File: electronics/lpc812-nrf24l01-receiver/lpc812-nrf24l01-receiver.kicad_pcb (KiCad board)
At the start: 2 copper layers, 25 x 24 mm, 21 parts, among them K1 BAT, K2 CH3, K3 TH, K4 ST, P1 NRF24L01+, SW1 ISP/BIND, U1 MCP1703T-3302E/CB, U2 LPC812M101JDH16_TSSOP16, X1 12 MHz

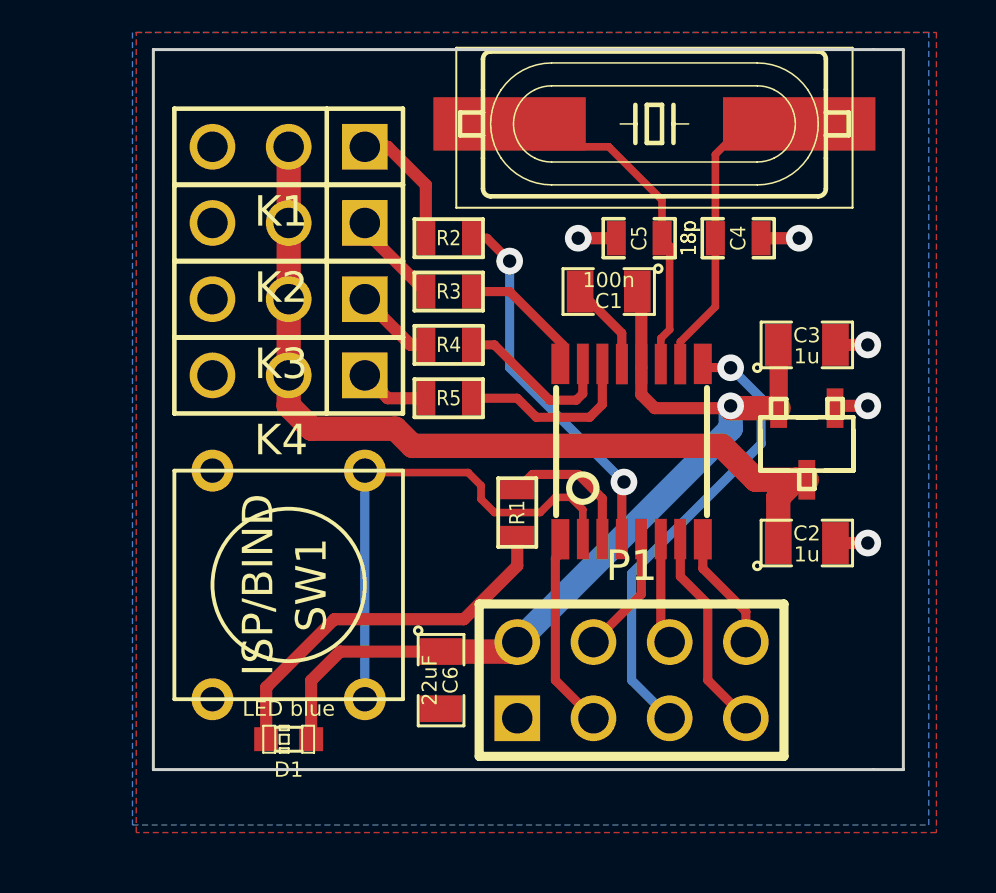
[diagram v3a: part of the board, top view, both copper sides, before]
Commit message: Start working on the silk screen
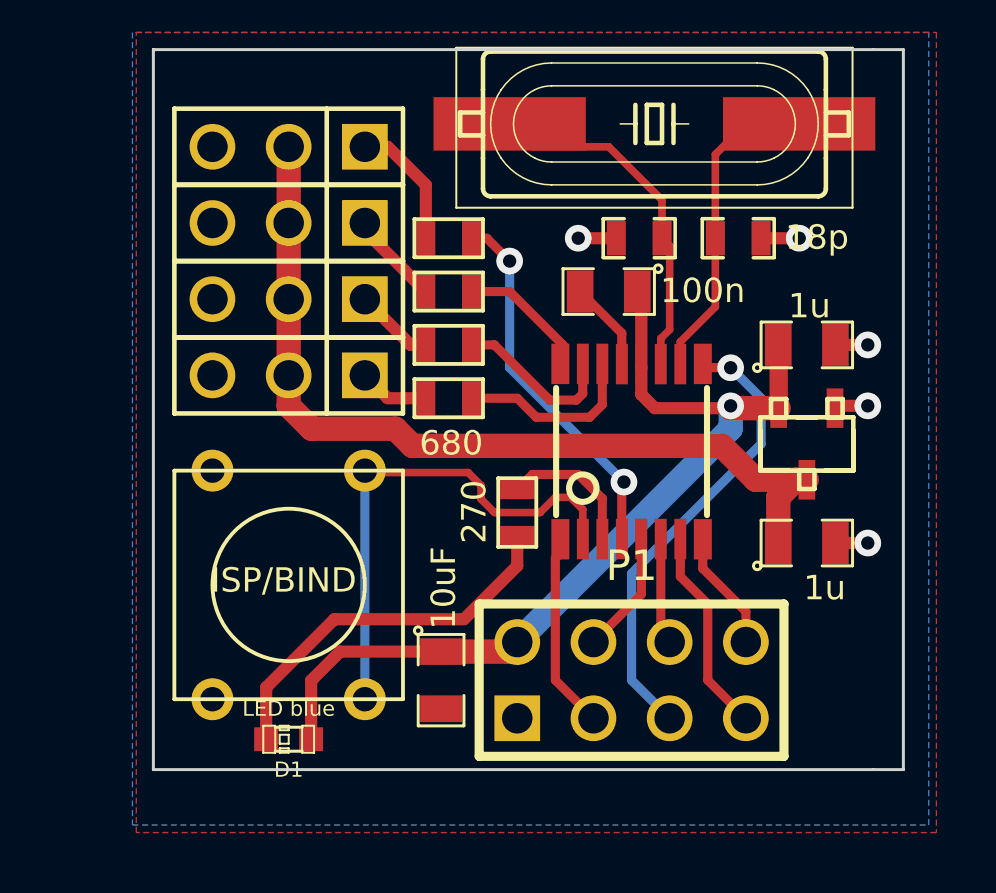
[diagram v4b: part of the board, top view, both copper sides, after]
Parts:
- C6: value 22uF -> 10uF
- U1: value MCP1703T-3302E/CB -> MCP1703
- U2: value LPC812M101JDH16_TSSOP16 -> LPC812
- X1: value 12 MHz -> 16 MHz
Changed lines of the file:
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@@
     (links 47)
     (no_connects 0)
-    (area 11.303 10.11555 55.524401 38.100001)
+    (area 55.372 10.16 96.592672 84.100001)
     (thickness 1.6)
     (drawings 6)
@@
     (22 B.Mask user)
     (23 F.Mask user)
-    (24 Dwgs.User user)
+    (24 Dwgs.User user hide)
     (25 Cmts.User user)
     (26 Eco1.User user)
@@
     (pad_to_mask_clearance 0)
     (aux_axis_origin 65 58)
-    (visible_elements 7FFFFFCF)
+    (visible_elements 7FFFFF9F)
     (pcbplotparams
       (layerselection 284721153)
@@
     (descr "Connecteur 3 pins")
     (tags "CONN DEV")
-    (fp_text reference K1 (at 0.254 -2.159 180) (layer F.SilkS)
+    (fp_text reference K1 (at 0.254 -2.159 180) (layer F.SilkS) hide
       (effects (font (size 1.016 1.016) (thickness 0.1524)))
     )
@@
     (descr "Connecteur 3 pins")
     (tags "CONN DEV")
-    (fp_text reference K2 (at 0.254 -2.159 180) (layer F.SilkS)
+    (fp_text reference K2 (at 0.254 -2.159 180) (layer F.SilkS) hide
       (effects (font (size 1.016 1.016) (thickness 0.1524)))
     )
@@
     (descr "Connecteur 3 pins")
     (tags "CONN DEV")
-    (fp_text reference K3 (at 0.254 -2.159 180) (layer F.SilkS)
+    (fp_text reference K3 (at 0.254 -2.159 180) (layer F.SilkS) hide
       (effects (font (size 1.016 1.016) (thickness 0.1524)))
     )
@@
     (descr "Connecteur 3 pins")
     (tags "CONN DEV")
-    (fp_text reference K4 (at 0.254 -2.159 180) (layer F.SilkS)
+    (fp_text reference K4 (at 0.254 -2.159 180) (layer F.SilkS) hide
       (effects (font (size 1.016 1.016) (thickness 0.1524)))
     )
@@
     (at 86.782 71.146 180)
     (attr smd)
-    (fp_text reference U1 (at 0.9652 -3.4544 180) (layer B.SilkS)
+    (fp_text reference U1 (at -7.198 -4.038 180) (layer B.SilkS) hide
       (effects (font (size 2.0828 2.0828) (thickness 0.0889)))
     )
-    (fp_text value MCP1703T-3302E/CB (at 0.5588 3.3782 180) (layer B.SilkS)
-      (effects (font (size 2.0828 2.0828) (thickness 0.0889)))
+    (fp_text value MCP1703 (at -2.372 0.026 270) (layer B.SilkS)
+      (effects (font (size 0.8128 0.8128) (thickness 0.2032)))
     )
     (fp_line (start -0.6858 0.889) (end -1.1938 0.889) (layer F.SilkS) (width 0.1524))
@@
     (at 84.496 64.288)
     (attr smd)
-    (fp_text reference C4 (at 0 0 90) (layer F.SilkS)
+    (fp_text reference C4 (at 0 0 90) (layer F.SilkS) hide
       (effects (font (size 0.508 0.4572) (thickness 0.1143)))
     )
-    (fp_text value 18p (at -1.651 0 90) (layer F.SilkS)
-      (effects (font (size 0.508 0.4572) (thickness 0.1143)))
+    (fp_text value 18p (at 2.626 -0.026) (layer F.SilkS)
+      (effects (font (size 0.8128 0.8128) (thickness 0.2032)))
     )
     (fp_line (start 0.50038 0.65024) (end 1.19888 0.65024) (layer F.SilkS) (width 0.11938))
@@
     (at 81.194 64.288 180)
     (attr smd)
-    (fp_text reference C5 (at 0 0 270) (layer F.SilkS)
-      (effects (font (size 0.508 0.4572) (thickness 0.1143)))
-    )
-    (fp_text value 18p (at -1.651 0 270) (layer F.SilkS)
-      (effects (font (size 0.508 0.4572) (thickness 0.1143)))
+    (fp_text reference C5 (at 0 0 270) (layer F.SilkS) hide
+      (effects (font (size 0.8128 0.8128) (thickness 0.000001)))
+    )
+    (fp_text value 18p (at -1.651 0 270) (layer F.SilkS) hide
+      (effects (font (size 0.8128 0.8128) (thickness 0.2032)))
     )
     (fp_line (start 0.50038 0.65024) (end 1.19888 0.65024) (layer F.SilkS) (width 0.11938))
@@
   (module SW_PUSH_SMALL (layer F.Cu)
     (at 69.51 75.845 270)
-    (fp_text reference SW1 (at 0 -0.762 270) (layer F.SilkS)
+    (fp_text reference SW1 (at 0 -0.762 270) (layer F.SilkS) hide
       (effects (font (size 1.016 1.016) (thickness 0.2032)))
     )
-    (fp_text value ISP/BIND (at 0 1.016 270) (layer F.SilkS)
-      (effects (font (size 1.016 1.016) (thickness 0.2032)))
+    (fp_text value ISP/BIND (at -0.153 0.168 360) (layer F.SilkS)
+      (effects (font (size 0.8128 0.8128) (thickness 0.2032)))
     )
     (fp_circle (center 0 0) (end 0 -2.54) (layer F.SilkS) (width 0.127))
@@
     (tags CRYSTAL)
     (attr smd)
-    (fp_text reference X1 (at -2.54 -3.302 180) (layer B.SilkS)
+    (fp_text reference X1 (at -2.54 -3.302 180) (layer B.SilkS) hide
       (effects (font (size 1.27 1.27) (thickness 0.0889)))
     )
-    (fp_text value "12 MHz" (at -1.905 3.429 180) (layer B.SilkS)
-      (effects (font (size 1.27 1.27) (thickness 0.0889)))
+    (fp_text value "16 MHz" (at 0.168 -1.752 180) (layer B.SilkS)
+      (effects (font (size 0.8128 0.8128) (thickness 0.2032)))
     )
     (fp_line (start -6.604 2.54) (end 6.604 2.54) (layer F.SilkS) (width 0.06604))
@@
     (at 74.59 79.02 270)
     (attr smd)
-    (fp_text reference C6 (at 0 -0.3175 270) (layer F.SilkS)
+    (fp_text reference C6 (at 0 -0.3175 270) (layer F.SilkS) hide
       (effects (font (size 0.50038 0.50038) (thickness 0.10922)))
     )
-    (fp_text value 22uF (at 0 0.381 270) (layer F.SilkS)
-      (effects (font (size 0.50038 0.50038) (thickness 0.10922)))
+    (fp_text value 10uF (at -3.074 -0.086 270) (layer F.SilkS)
+      (effects (font (size 0.8128 0.8128) (thickness 0.2032)))
     )
     (fp_circle (center -1.651 0.762) (end -1.651 0.635) (layer F.SilkS) (width 0.09906))
@@
     (at 74.844 64.288 180)
     (attr smd)
-    (fp_text reference R2 (at 0 0 180) (layer F.SilkS)
+    (fp_text reference R2 (at 0 0 180) (layer F.SilkS) hide
       (effects (font (size 0.508 0.4572) (thickness 0.1143)))
     )
@@
     (at 74.844 66.066 180)
     (attr smd)
-    (fp_text reference R3 (at 0 0 180) (layer F.SilkS)
+    (fp_text reference R3 (at 0 0 180) (layer F.SilkS) hide
       (effects (font (size 0.508 0.4572) (thickness 0.1143)))
     )
@@
     (at 74.844 67.844 180)
     (attr smd)
-    (fp_text reference R4 (at 0 0 180) (layer F.SilkS)
+    (fp_text reference R4 (at 0 0 180) (layer F.SilkS) hide
       (effects (font (size 0.508 0.4572) (thickness 0.1143)))
     )
@@
     (at 74.844 69.622 180)
     (attr smd)
-    (fp_text reference R5 (at 0 0 180) (layer F.SilkS)
+    (fp_text reference R5 (at 0 0 180) (layer F.SilkS) hide
       (effects (font (size 0.508 0.4572) (thickness 0.1143)))
     )
-    (fp_text value 680 (at 0 0 180) (layer F.SilkS) hide
-      (effects (font (size 0.508 0.4572) (thickness 0.1143)))
+    (fp_text value 680 (at -0.086 -1.498 180) (layer F.SilkS)
+      (effects (font (size 0.8128 0.8128) (thickness 0.2032)))
     )
     (fp_line (start -1.143 -0.635) (end 1.143 -0.635) (layer F.SilkS) (width 0.127))
@@
     (at 86.782 67.844)
     (attr smd)
-    (fp_text reference C3 (at 0 -0.3175) (layer F.SilkS)
-      (effects (font (size 0.50038 0.50038) (thickness 0.10922)))
-    )
-    (fp_text value 1u (at 0 0.381) (layer F.SilkS)
-      (effects (font (size 0.50038 0.50038) (thickness 0.10922)))
+    (fp_text reference C3 (at 0 -0.3175) (layer F.SilkS) hide
+      (effects (font (size 0.8128 0.8128) (thickness 0.10922)))
+    )
+    (fp_text value 1u (at 0.086 -1.296) (layer F.SilkS)
+      (effects (font (size 0.8128 0.8128) (thickness 0.2032)))
     )
     (fp_circle (center -1.651 0.762) (end -1.651 0.635) (layer F.SilkS) (width 0.09906))
@@
     (at 80.178 66.066 180)
     (attr smd)
-    (fp_text reference C1 (at 0 -0.3175 180) (layer F.SilkS)
+    (fp_text reference C1 (at 0 -0.3175 180) (layer F.SilkS) hide
       (effects (font (size 0.50038 0.50038) (thickness 0.10922)))
     )
-    (fp_text value 100n (at 0 0.381 180) (layer F.SilkS)
-      (effects (font (size 0.50038 0.50038) (thickness 0.10922)))
+    (fp_text value 100n (at -3.134 0.026 180) (layer F.SilkS)
+      (effects (font (size 0.8128 0.8128) (thickness 0.2032)))
     )
     (fp_circle (center -1.651 0.762) (end -1.651 0.635) (layer F.SilkS) (width 0.09906))
@@
     (at 86.782 74.448)
     (attr smd)
-    (fp_text reference C2 (at 0 -0.3175) (layer F.SilkS)
+    (fp_text reference C2 (at 0 -0.3175) (layer F.SilkS) hide
       (effects (font (size 0.50038 0.50038) (thickness 0.10922)))
     )
-    (fp_text value 1u (at 0 0.381) (layer F.SilkS)
-      (effects (font (size 0.50038 0.50038) (thickness 0.10922)))
+    (fp_text value 1u (at 0.594 1.498) (layer F.SilkS)
+      (effects (font (size 0.8128 0.8128) (thickness 0.2032)))
     )
     (fp_circle (center -1.651 0.762) (end -1.651 0.635) (layer F.SilkS) (width 0.09906))
@@
     (at 77.13 73.432 90)
     (attr smd)
-    (fp_text reference R1 (at 0 0 90) (layer F.SilkS)
+    (fp_text reference R1 (at 0 0 90) (layer F.SilkS) hide
       (effects (font (size 0.508 0.4572) (thickness 0.1143)))
     )
-    (fp_text value 270 (at 0 0 90) (layer F.SilkS) hide
-      (effects (font (size 0.508 0.4572) (thickness 0.1143)))
+    (fp_text value 270 (at 0.026 -1.438 90) (layer F.SilkS)
+      (effects (font (size 0.8128 0.8128) (thickness 0.2032)))
     )
     (fp_line (start -1.143 -0.635) (end 1.143 -0.635) (layer F.SilkS) (width 0.127))
@@
     (at 80.94 71.4)
     (descr "<b>Thin Shrink Small Outline Plastic 16</b><p>")
-    (fp_text reference U2 (at -3.302 -0.3556 90) (layer Eco1.User)
+    (fp_text reference U2 (at -3.302 -0.3556 90) (layer Eco1.User) hide
       (effects (font (size 0.8128 0.8128) (thickness 0.14478)))
     )
-    (fp_text value LPC812M101JDH16_TSSOP16 (at 2.921 0.8636 90) (layer Eco1.User)
-      (effects (font (size 0.4064 0.4064) (thickness 0.04064)))
+    (fp_text value LPC812 (at -0.041 -0.153) (layer Eco1.User)
+      (effects (font (size 0.8128 0.8128) (thickness 0.2032)))
     )
     (fp_line (start -2.5146 2.28092) (end 2.5146 2.28092) (layer Cmts.User) (width 0.2032))

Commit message: Tweak the footprints and board
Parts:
- U1: value MCP1703 -> MCP1703T-3302E/CB
- U2: value LPC812 -> LPC812M101JDH16
- X1: footprint crystal-SM49 -> Q_49U3HMS
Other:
- net class Default: via_dia 0.889 -> 0.9; via_drill 0.635 -> 0.6

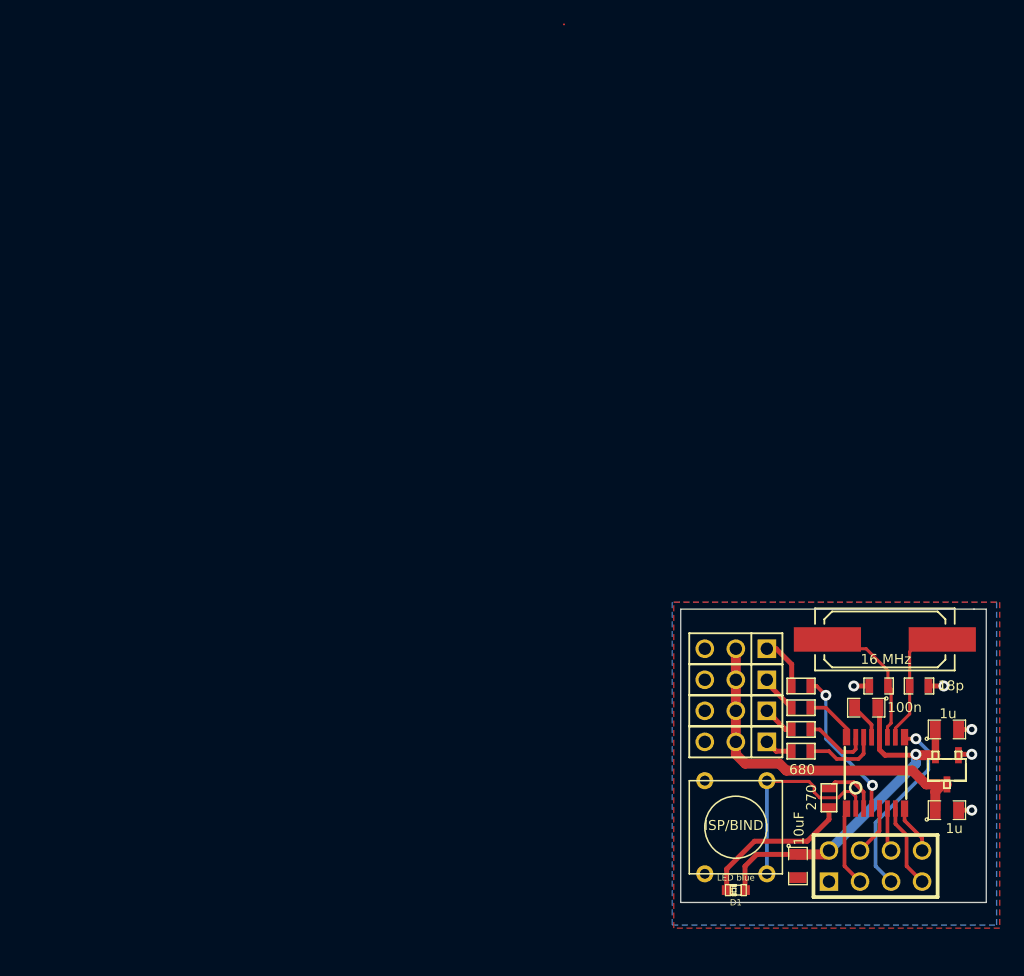
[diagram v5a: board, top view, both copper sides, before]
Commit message: More tweaking and playing around with silk screen and coordinates
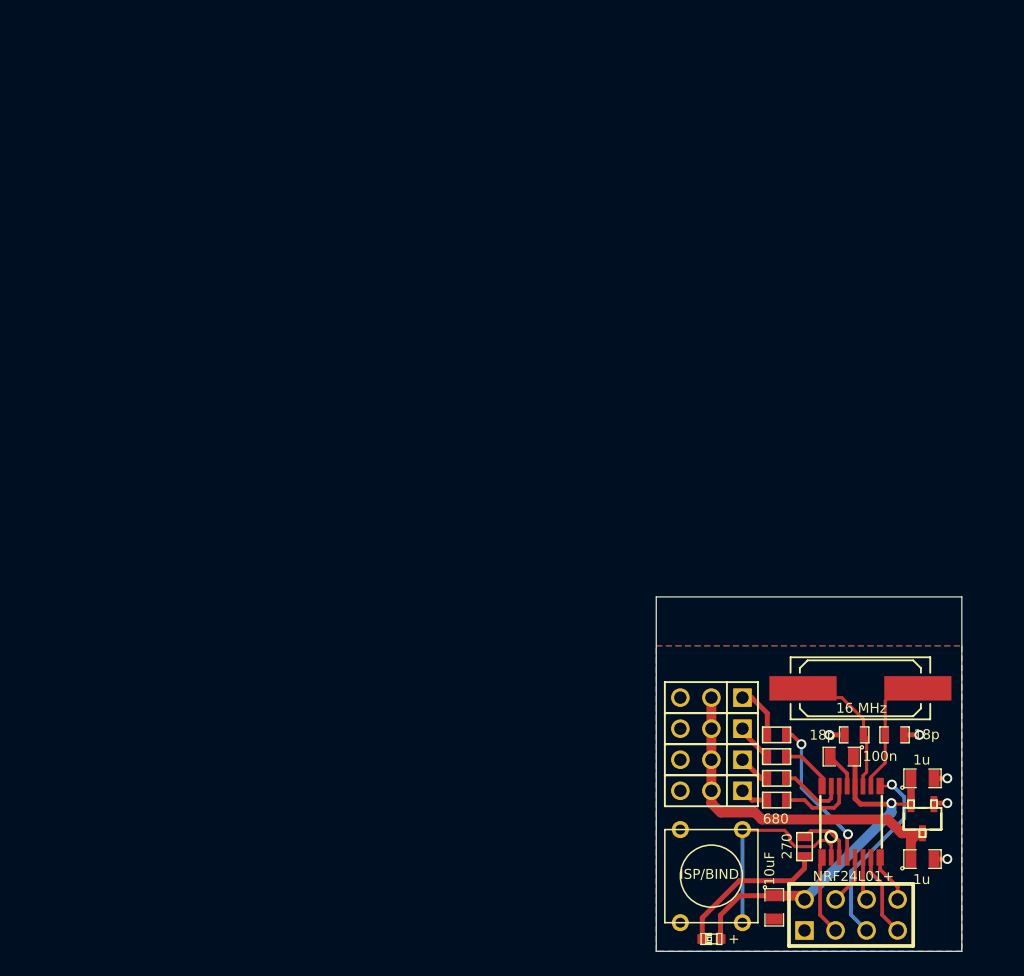
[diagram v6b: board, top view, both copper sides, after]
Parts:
- U1: value MCP1703T-3302E/CB -> MCP1703
- U2: value LPC812M101JDH16 -> LPC812
- moved C1 4.47 mm to (78.2, 70.1)
- moved C2 4.47 mm to (84.8, 78.4)
- moved C3 4.47 mm to (84.8, 71.8)
- moved C4 4.47 mm to (82.5, 68.3)
- moved C5 4.47 mm to (79.2, 68.3)
- moved D1 4.47 mm to (67.5, 85.0)
- moved K2 4.47 mm to (67.5, 67.8)
- moved K3 4.47 mm to (67.5, 70.3)
- moved K4 4.47 mm to (67.5, 72.9)
- moved P1 4.47 mm to (78.9, 83.0)
- moved R1 4.47 mm to (75.1, 77.4)
- moved R2 4.47 mm to (72.8, 68.3)
- moved R3 4.47 mm to (72.8, 70.1)
- moved R4 4.47 mm to (72.8, 71.8)
- moved R5 4.47 mm to (72.8, 73.6)
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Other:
- board size 25 x 24 mm -> 25 x 29 mm
- net class Default: clearance 0.254 -> 0.2032; via_dia 0.9 -> 0.813; via_drill 0.6 -> 0.5
- rule trace_clearance: 0.254 -> 0.2032
- rule via_min_drill: 0.508 -> 0.3048
- rule via_min_size: 0.508 -> 0.6096
- board text added: "+"
- board text added: "LANE Boys RC"
- board text added: "nRF24 surface receiver"
